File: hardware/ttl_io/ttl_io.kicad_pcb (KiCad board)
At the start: 4 copper layers, 80 x 50 mm, 135 parts, among them J1 Conn_Coaxial, J2 Conn_01x03_Male, J3 Conn_Triaxial, J3 USB_C_Receptacle_USB2.0, J4 AudioJack3, J6 Barrel_Jack_Switch, J7 Conn_Coaxial, SW1 SW_Push, U1 74LVCH2T45DC, U11 LM27762, U12 LT3030, U13 ADS7049, U2 TPD2EUSB30, U3 ADUM4160, U4 RP2040, U5 W25Q16JVUXIQ, U6 LTC6263, U7 LTC6268xS8-10, U8 REF3433QDBVRQ1, U9 AD9833xRM, X1 ECS-TXO-2016

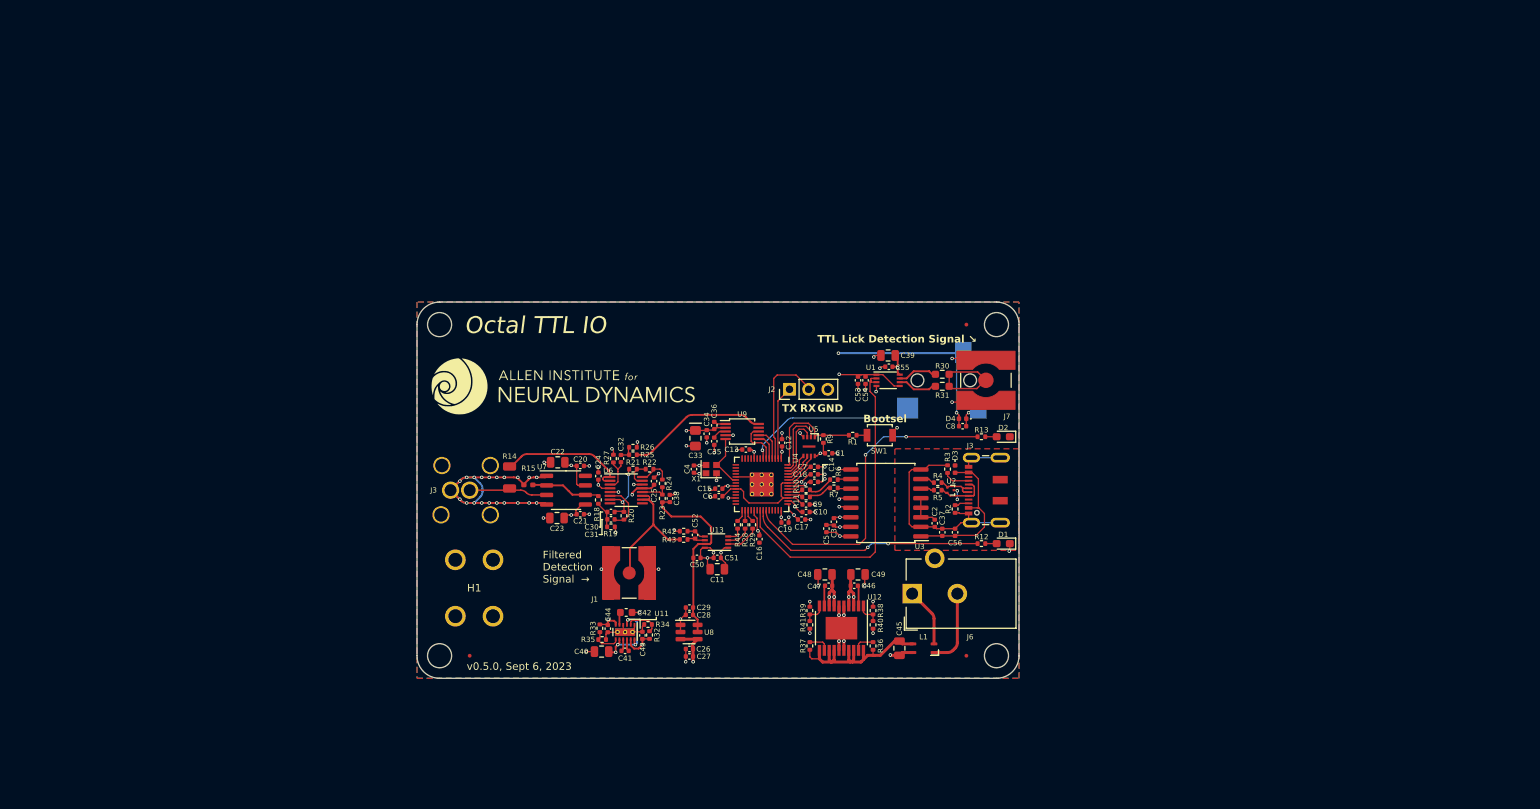
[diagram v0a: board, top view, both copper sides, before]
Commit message: update passthrough level translator
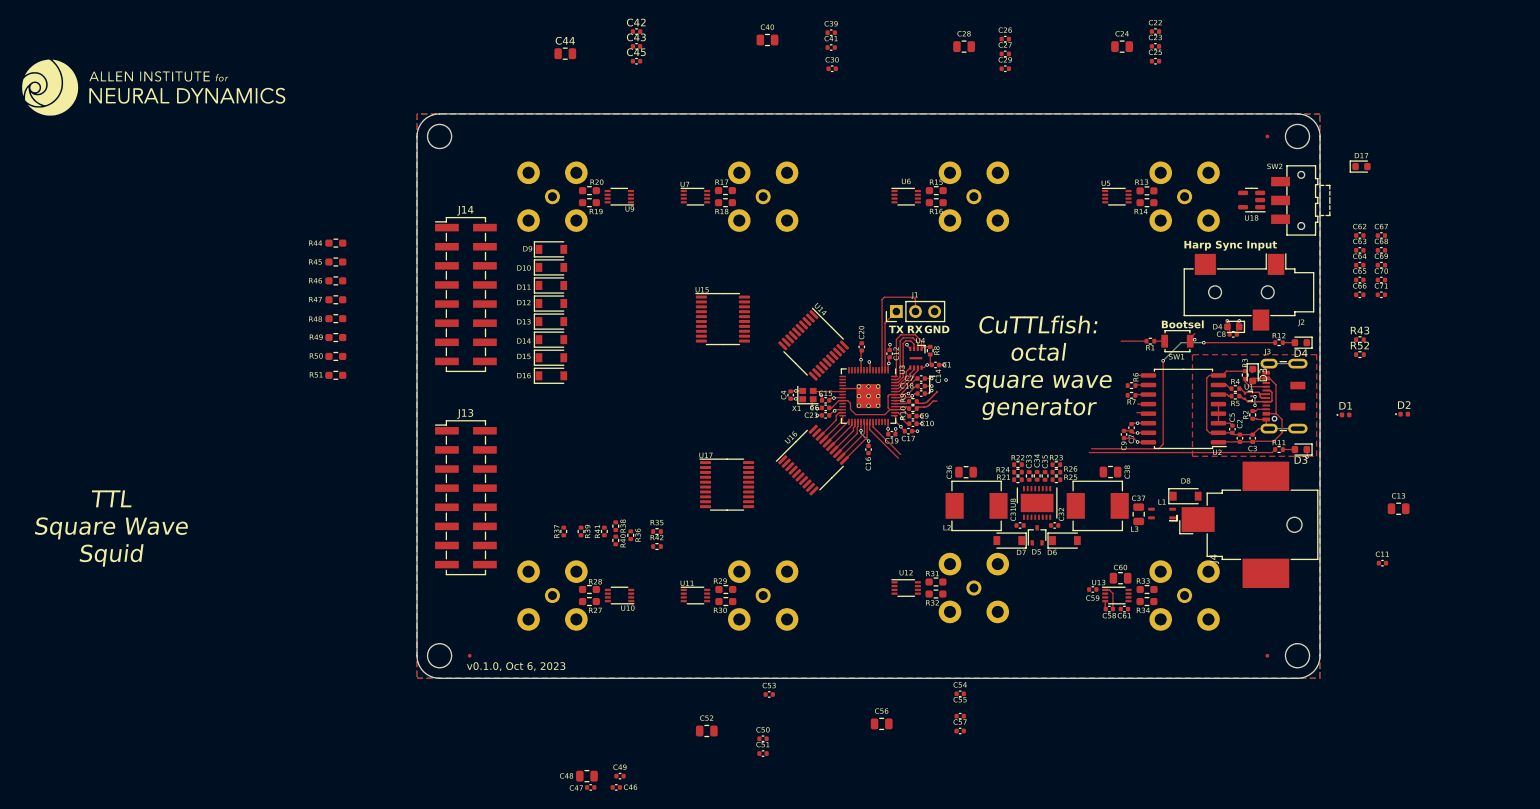
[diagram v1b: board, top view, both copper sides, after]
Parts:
- removed the C20 at (126.6, 89.8)
- removed G1: LOGO, LOGO
- removed H1: MountingHole_Pad, kicad_component_library:Terminal_Keystone_779x_EdgeMount_Horizontal
- removed the J2 at (154.4, 79.6)
- removed the J3 at (111.9, 93.0)
- removed the REF** at (181.9, 115.0)
- removed the REF** at (181.9, 71.0)
- removed the REF** at (107.9, 71.0)
- removed the REF** at (107.9, 115.0)
- removed REF1: OSHW-Logo2_7.3x6mm_SilkScreen, Symbol:OSHW-Logo2_7.3x6mm_SilkScreen
- removed the U1 at (167.5, 78.4)
- added C13: 10uF, Capacitor_SMD:C_0805_2012Metric, F.Cu at (235.3, 95.5)
- added C45: 100nF, Capacitor_SMD:C_0402_1005Metric, F.Cu at (134.1, 36.0)
- added C56: 10uF, Capacitor_SMD:C_0805_2012Metric, F.Cu at (166.7, 124.1)
- added C57: 100nF, Capacitor_SMD:C_0402_1005Metric, F.Cu at (177.1, 125.0)
- added C58: 100nF, Capacitor_SMD:C_0402_1005Metric, F.Cu at (196.9, 108.8)
- added C59: 1uF, Capacitor_SMD:C_0402_1005Metric, F.Cu at (194.7, 106.2)
- added C60: 10uF, Capacitor_SMD:C_0805_2012Metric, F.Cu at (198.4, 104.7)
- added C61: 100nF, Capacitor_SMD:C_0402_1005Metric, F.Cu at (198.9, 108.8)
- added C62: 100nF, Capacitor_SMD:C_0402_1005Metric, F.Cu at (230.2, 59.2)
- added C63: 1uF, Capacitor_SMD:C_0402_1005Metric, F.Cu at (230.2, 61.1)
- added C64: 100nF, Capacitor_SMD:C_0402_1005Metric, F.Cu at (230.2, 63.1)
- added C65: 1uF, Capacitor_SMD:C_0402_1005Metric, F.Cu at (230.2, 65.1)
- added C66: 100nF, Capacitor_SMD:C_0402_1005Metric, F.Cu at (230.2, 67.0)
- added C67: 1uF, Capacitor_SMD:C_0402_1005Metric, F.Cu at (233.1, 59.2)
- added C68: 100nF, Capacitor_SMD:C_0402_1005Metric, F.Cu at (233.1, 61.1)
- added C69: 1uF, Capacitor_SMD:C_0402_1005Metric, F.Cu at (233.1, 63.1)
- added C70: 100nF, Capacitor_SMD:C_0402_1005Metric, F.Cu at (233.1, 65.1)
- added C71: 1uF, Capacitor_SMD:C_0402_1005Metric, F.Cu at (233.1, 67.0)
- added D1: D_TVS, Diode_SMD:D_0402_1005Metric, F.Cu at (228.3, 83.0)
- added D10: D_Schottky, Diode_SMD:D_SOD-123, F.Cu at (122.8, 63.4)
- added D11: D_Schottky, Diode_SMD:D_SOD-123, F.Cu at (122.8, 65.8)
- added D12: D_Schottky, Diode_SMD:D_SOD-123, F.Cu at (122.8, 68.2)
- added D13: D_Schottky, Diode_SMD:D_SOD-123, F.Cu at (122.8, 70.6)
- added D14: D_Schottky, Diode_SMD:D_SOD-123, F.Cu at (122.8, 73.0)
- added D15: D_Schottky, Diode_SMD:D_SOD-123, F.Cu at (122.8, 75.4)
- added D16: D_Schottky, Diode_SMD:D_SOD-123, F.Cu at (122.8, 77.8)
- added D17: LED, LED_SMD:LED_0603_1608Metric, F.Cu at (230.4, 50.0)
- added D2: D_TVS, Diode_SMD:D_0402_1005Metric, F.Cu at (236.1, 82.9)
- added D5: BAT54AW, Package_TO_SOT_SMD:SOT-323_SC-70, F.Cu at (187.3, 99.0)
- added D6: D_Schottky, Diode_SMD:D_SOD-123, F.Cu at (191.0, 99.7)
- added D7: D_Schottky, Diode_SMD:D_SOD-123, F.Cu at (183.6, 99.7)
- added D8: D_Schottky, Diode_SMD:D_SOD-123, F.Cu at (207.1, 93.8)
- added D9: D_Schottky, Diode_SMD:D_SOD-123, F.Cu at (122.8, 61.0)
- added J10: Conn_Coaxial, kicad_component_library:BNC_TEConnectivity_CONBNC001_Vertical, B.Cu at (150.9, 107.0)
- added J11: Conn_Coaxial, kicad_component_library:BNC_TEConnectivity_CONBNC001_Vertical, B.Cu at (178.9, 106.0)
- added J12: Conn_Coaxial, kicad_component_library:BNC_TEConnectivity_CONBNC001_Vertical, B.Cu at (206.9, 107.0)
- added J13: Conn_02x08_Counter_Clockwise, Connector_PinHeader_2.54mm:PinHeader_2x08_P2.54mm_Vertical_SMD, F.Cu at (111.4, 94.0)
- added J14: Conn_02x08_Counter_Clockwise, Connector_PinHeader_2.54mm:PinHeader_2x08_P2.54mm_Vertical_SMD, F.Cu at (111.4, 67.0)
- added J5: Conn_Coaxial, kicad_component_library:BNC_TEConnectivity_CONBNC001_Vertical, B.Cu at (206.9, 54.0)
- added J6: Conn_Coaxial, kicad_component_library:BNC_TEConnectivity_CONBNC001_Vertical, B.Cu at (178.9, 54.0)
- added J8: Conn_Coaxial, kicad_component_library:BNC_TEConnectivity_CONBNC001_Vertical, B.Cu at (122.9, 54.0)
- added J9: Conn_Coaxial, kicad_component_library:BNC_TEConnectivity_CONBNC001_Vertical, B.Cu at (122.9, 107.0)
- added L2: 10uH, Inductor_SMD:L_Vishay_IHLP-2525, F.Cu at (179.3, 95.1)
- added L3: 10uH, Inductor_SMD:L_Vishay_IHLP-2525, F.Cu at (195.4, 95.1)
- added R13: 100, Resistor_SMD:R_0603_1608Metric_Pad0.98x0.95mm_HandSolder, F.Cu at (201.9, 53.2)
- added R16: 100, Resistor_SMD:R_0603_1608Metric_Pad0.98x0.95mm_HandSolder, F.Cu at (173.9, 54.8)
- added R17: 100, Resistor_SMD:R_0603_1608Metric_Pad0.98x0.95mm_HandSolder, F.Cu at (145.9, 53.2)
- added R45: 100, Resistor_SMD:R_0603_1608Metric_Pad0.98x0.95mm_HandSolder, F.Cu at (94.1, 62.7)
- added R46: 100, Resistor_SMD:R_0603_1608Metric_Pad0.98x0.95mm_HandSolder, F.Cu at (94.1, 65.2)
- added R47: 100, Resistor_SMD:R_0603_1608Metric_Pad0.98x0.95mm_HandSolder, F.Cu at (94.1, 67.7)
- added R48: 100, Resistor_SMD:R_0603_1608Metric_Pad0.98x0.95mm_HandSolder, F.Cu at (94.1, 70.2)
- added R49: 100, Resistor_SMD:R_0603_1608Metric_Pad0.98x0.95mm_HandSolder, F.Cu at (94.1, 72.7)
- added R50: 100, Resistor_SMD:R_0603_1608Metric_Pad0.98x0.95mm_HandSolder, F.Cu at (94.1, 75.2)
- added R51: 100, Resistor_SMD:R_0603_1608Metric_Pad0.98x0.95mm_HandSolder, F.Cu at (94.1, 77.7)
- added R52: 1K, Resistor_SMD:R_0402_1005Metric, F.Cu at (230.2, 75.0)
- added REF**: MountingHole_3.2mm_M3_ISO7380, MountingHole:MountingHole_3.2mm_M3_ISO7380, F.Cu at (107.9, 46.0)
- added REF**: MountingHole_3.2mm_M3_ISO7380, MountingHole:MountingHole_3.2mm_M3_ISO7380, F.Cu at (221.9, 46.0)
- added REF**: MountingHole_3.2mm_M3_ISO7380, MountingHole:MountingHole_3.2mm_M3_ISO7380, F.Cu at (107.9, 115.0)
- added REF**: MountingHole_3.2mm_M3_ISO7380, MountingHole:MountingHole_3.2mm_M3_ISO7380, F.Cu at (221.9, 115.0)
- added SW2: SW_SPDT, Button_Switch_SMD:SW_SPDT_CK-JS102011SAQN, F.Cu at (222.4, 54.5)
- added U10: 74LVCH2T45DC, Package_SO:VSSOP-8_2.3x2mm_P0.5mm, F.Cu at (131.8, 107.0)
- added U14: 74CBTLV3245, Package_SO:TSSOP-20_4.4x6.5mm_P0.65mm, F.Cu at (157.6, 73.8)
- added U15: 74CBTLV3245, Package_SO:TSSOP-20_4.4x6.5mm_P0.65mm, F.Cu at (145.6, 70.3)
- added U16: 74CBTLV3245, Package_SO:TSSOP-20_4.4x6.5mm_P0.65mm, F.Cu at (157.6, 89.0)
- added U17: 74CBTLV3245, Package_SO:TSSOP-20_4.4x6.5mm_P0.65mm, F.Cu at (146.1, 92.3)
- added U18: 74LVC1G04, Package_TO_SOT_SMD:SOT-23-5, F.Cu at (215.8, 54.5)
- added U5: 74LVCH2T45DC, Package_SO:VSSOP-8_2.3x2mm_P0.5mm, F.Cu at (197.9, 54.0)
- C11, C23, C39: value 10uF -> 1uF; footprint Capacitor_SMD:C_0805_2012Metric -> Capacitor_SMD:C_0402_1005Metric
- C12, C55: value 100nF -> 1uF
- C2: renamed from C37; value 100nF -> 1uF
- C22: value 10uF -> 100nF; footprint Capacitor_SMD:C_0805_2012Metric -> Capacitor_SMD:C_0402_1005Metric
- C24, C28: value 100nF -> 10uF; footprint Capacitor_SMD:C_0402_1005Metric -> Capacitor_SMD:C_0805_2012Metric
- C29, C41, C53, C8, C9: value 1uF -> 100nF
- C3: renamed from C56; value 1uF -> 100nF
- C30, C31: value 160pF -> 100nF
- C32, C46: value 10nF -> 100nF
- C33: value 10uF -> 1.5nF; footprint Capacitor_SMD:C_0805_2012Metric_Pad1.18x1.45mm_HandSolder -> Resistor_SMD:R_0402_1005Metric
- C34: value 100nF -> 4.7nF; footprint Capacitor_SMD:C_0402_1005Metric -> Resistor_SMD:R_0402_1005Metric
- C35: value 100nF -> 1.5nF; footprint Capacitor_SMD:C_0402_1005Metric -> Resistor_SMD:R_0402_1005Metric
- C36: value 10nF -> 22uF; footprint Capacitor_SMD:C_0402_1005Metric -> Capacitor_SMD:C_0805_2012Metric
- C37: renamed from C45; value 3.3uF -> 10uF
- C38: value 100nF -> 22uF; footprint Capacitor_SMD:C_0402_1005Metric -> Capacitor_SMD:C_0805_2012Metric
- C40: value 22uF -> 10uF
- C42: value 4.7uF -> 100nF; footprint Capacitor_SMD:C_0603_1608Metric -> Capacitor_SMD:C_0402_1005Metric
- C43, C51: value 2.2uF -> 1uF
- C44: value 2.2uF -> 10uF; footprint Capacitor_SMD:C_0402_1005Metric -> Capacitor_SMD:C_0805_2012Metric
- C47: value 10nF -> 1uF
- C49: value 22uF -> 100nF; footprint Capacitor_SMD:C_0805_2012Metric -> Capacitor_SMD:C_0402_1005Metric
- C50: value 2.2uF -> 100nF
- C52: value 300pF -> 10uF; footprint Capacitor_SMD:C_0402_1005Metric -> Capacitor_SMD:C_0805_2012Metric
- D3: renamed from D1; footprint LED_SMD:LED_0603_1608Metric_Pad1.05x0.95mm_HandSolder -> LED_SMD:LED_0603_1608Metric
- D3, D4: value D_TVS -> LED; footprint Diode_SMD:D_0402_1005Metric -> LED_SMD:LED_0603_1608Metric
- D4: renamed from D2; footprint LED_SMD:LED_0603_1608Metric_Pad1.05x0.95mm_HandSolder -> LED_SMD:LED_0603_1608Metric
- J1: value Conn_Coaxial -> Conn_01x03_Male; footprint Connector_Coaxial:SMA_Amphenol_132134-10_Vertical -> Connector_PinHeader_2.54mm:PinHeader_1x03_P2.54mm_Vertical
- J2: renamed from J4; moved to F.Cu
- J4: renamed from J6; footprint Connector_BarrelJack:BarrelJack_CUI_PJ-102AH_Horizontal -> Connector_BarrelJack:BarrelJack_CUI_PJ-036AH-SMT_Horizontal
- J7: footprint kicad_component_library:SMA_TE_Connectivity_CONSMA002-SMD-G-T_Horizontal -> kicad_component_library:BNC_TEConnectivity_CONBNC001_Vertical; moved to B.Cu
- R11: renamed from R12; value 330 -> 680
- R12: renamed from R13; value 330 -> 680
- R14: value 100K -> 100; footprint Resistor_SMD:R_1206_3216Metric -> Resistor_SMD:R_0603_1608Metric_Pad0.98x0.95mm_HandSolder
- R15: footprint Resistor_SMD:R_0402_1005Metric_Pad0.72x0.64mm_HandSolder -> Resistor_SMD:R_0603_1608Metric_Pad0.98x0.95mm_HandSolder
- R18: value 49K9 -> 100; footprint Resistor_SMD:R_0402_1005Metric -> Resistor_SMD:R_0603_1608Metric_Pad0.98x0.95mm_HandSolder
- R19: value 1K02 -> 100; footprint Resistor_SMD:R_0402_1005Metric -> Resistor_SMD:R_0603_1608Metric_Pad0.98x0.95mm_HandSolder
- R20: value 100K -> 100; footprint Resistor_SMD:R_0402_1005Metric -> Resistor_SMD:R_0603_1608Metric_Pad0.98x0.95mm_HandSolder
- R21: value 68 -> 10K
- R24: value 10K -> 31K2
- R26: value 330 -> 52K3
- R27: value 10K -> 100; footprint Resistor_SMD:R_0402_1005Metric -> Resistor_SMD:R_0603_1608Metric_Pad0.98x0.95mm_HandSolder
- R28, R29, R44: value 49.9 -> 100; footprint Resistor_SMD:R_0402_1005Metric -> Resistor_SMD:R_0603_1608Metric_Pad0.98x0.95mm_HandSolder
- R32: value 54K9 -> 100; footprint Resistor_SMD:R_0402_1005Metric -> Resistor_SMD:R_0603_1608Metric_Pad0.98x0.95mm_HandSolder
- R33: value 53K6 -> 100; footprint Resistor_SMD:R_0402_1005Metric -> Resistor_SMD:R_0603_1608Metric_Pad0.98x0.95mm_HandSolder
- R34: value 51K -> 100; footprint Resistor_SMD:R_0402_1005Metric -> Resistor_SMD:R_0603_1608Metric_Pad0.98x0.95mm_HandSolder
- R35: value 51K -> 10K
- R36, R37: value 1M -> 10K
- R38: value 309K -> 10K
- R39: value 172K -> 10K
- R40, R41: value 100K -> 10K
- R42, R43: value 16 -> 10K
- U11: value LM27762 -> 74LVCH2T45DC; footprint Package_SON:WSON-12-1EP_3x2mm_P0.5mm_EP1x2.65_ThermalVias -> Package_SO:VSSOP-8_2.3x2mm_P0.5mm
- U12: value LT3030 -> 74LVCH2T45DC; footprint Package_SO:ETSSOP-20-1EP_4.4x6.5mm_P0.65mm_EP3x4.2mm -> Package_SO:VSSOP-8_2.3x2mm_P0.5mm
- U13: value ADS7049 -> 74LVCH2T45DC
- U6: value LTC6263 -> 74LVCH2T45DC; footprint Package_SO:MSOP-16_3x4mm_P0.5mm -> Package_SO:VSSOP-8_2.3x2mm_P0.5mm
- U7: value LTC6268xS8-10 -> 74LVCH2T45DC; footprint Package_SO:SO-8_3.9x4.9mm_P1.27mm -> Package_SO:VSSOP-8_2.3x2mm_P0.5mm
- U8: value REF3433QDBVRQ1 -> LT3506; footprint Package_TO_SOT_SMD:SOT-23-6 -> Package_DFN_QFN:DFN-16-1EP_4x5mm_P0.5mm_EP2.44x4.34mm
- U9: value AD9833xRM -> 74LVCH2T45DC; footprint Package_SO:MSOP-10_3x3mm_P0.5mm -> Package_SO:VSSOP-8_2.3x2mm_P0.5mm
- moved C23 101.3 mm to (203.0, 34.0), turned to 0 degrees
- moved C22 97.9 mm to (203.0, 32.1)
- moved R43 93.7 mm to (230.2, 73.0)
- moved R14 92.2 mm to (201.9, 54.8), turned to 0 degrees
- moved C26 91.3 mm to (183.1, 33.1)
- moved C27 90.4 mm to (183.1, 35.0), turned to 0 degrees
- moved C24 90.0 mm to (198.6, 34.1), turned to 0 degrees
- moved C11 88.4 mm to (233.2, 102.7), turned to 0 degrees
- moved C25 86.9 mm to (203.0, 36.0), turned to 0 degrees
- moved C41 84.7 mm to (159.9, 34.2), turned to 0 degrees
- moved C40 84.2 mm to (151.5, 33.2), turned to 0 degrees
- moved C28 83.9 mm to (177.6, 34.1)
- moved C29 83.0 mm to (183.1, 37.0), turned to 0 degrees
- moved C43 78.3 mm to (134.1, 34.0), turned to 0 degrees
- moved C42 77.2 mm to (134.1, 32.1)
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- renumbered C13 to C20, C2 to C5, C3 to C7, C5 to C9, R11 to R10, R9 to R8, R10 to R9, U2 to U1, U3 to U2, U4 to U3, U5 to U4
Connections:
- net /Harp Core RP2040 + Isolated USB/D+ renamed /Harp Core Rp2040 + isolated USB/D+
- net /Harp Core RP2040 + Isolated USB/D- renamed /Harp Core Rp2040 + isolated USB/D-
- net /Harp Core RP2040 + Isolated USB/DD+ renamed /Harp Core Rp2040 + isolated USB/DD+
- net /Harp Core RP2040 + Isolated USB/DD- renamed /Harp Core Rp2040 + isolated USB/DD-
- net /Harp Core RP2040 + Isolated USB/HARP_CLK_SYNC renamed /Harp Core Rp2040 + isolated USB/HARP_CLK_SYNC
- net /Harp Core RP2040 + Isolated USB/QSPI_CLK renamed /Harp Core Rp2040 + isolated USB/QSPI_CLK
- net /Harp Core RP2040 + Isolated USB/QSPI_CS renamed /Harp Core Rp2040 + isolated USB/QSPI_CS
- net /Harp Core RP2040 + Isolated USB/QSPI_D0 renamed /Harp Core Rp2040 + isolated USB/QSPI_D0
- net /Harp Core RP2040 + Isolated USB/QSPI_D1 renamed /Harp Core Rp2040 + isolated USB/QSPI_D1
- net /Harp Core RP2040 + Isolated USB/QSPI_D2 renamed /Harp Core Rp2040 + isolated USB/QSPI_D2
- net /Harp Core RP2040 + Isolated USB/QSPI_D3 renamed /Harp Core Rp2040 + isolated USB/QSPI_D3
- net /Harp Core RP2040 + Isolated USB/USB_Boot renamed /Harp Core Rp2040 + isolated USB/USB_Boot
- net /Harp Core RP2040 + Isolated USB/VDD1 renamed /Harp Core Rp2040 + isolated USB/VDD1
- C10 pad 1: +3V3 -> +1V1
- C12 pad 1: GND -> +3V3
- C12 pad 2: +3V3 -> GND
- C2 pad 1: GND1 -> VBUS
- C2 pad 2: VBUS -> GND1
- C21 pad 1: -2V5 -> GND
- C21 pad 2: GND -> +3V3
- C22 pad 2: +2V5 -> +3V3
- C23 pad 1: -2V5 -> +3V3
- C24 pad 1: GND -> +5V
- C24 pad 2: +2V5 -> GND
- C25 pad 1: -2V5 -> GND
- C25 pad 2: GND -> +5V
- C26 pad 2: +5V -> +3V3
- C27 pad 1: +5V -> +3V3
- C28 pad 1: GND -> +5V
- C28 pad 2: VREF_3V3 -> GND
- C29 pad 1: VREF_3V3 -> GND
- C29 pad 2: GND -> +5V
- C3 pad 1: VBUS -> GND1
- C3 pad 2: GND1 -> VBUS
- C30 pad 1: Net-(C30-Pad1) -> GND
- C30 pad 2: Net-(C30-Pad2) -> +3V3
- C31 pad 1: Net-(C30-Pad1) -> Net-(D7-K)
- C31 pad 2: Net-(U6B--) -> Net-(U8-BOOST1)
- C32 pad 1: Net-(C32-Pad1) -> Net-(D6-K)
- C32 pad 2: Net-(U6A-+) -> Net-(U8-BOOST2)
- C33 pad 1: +3V3 -> Net-(C33-Pad1)
- C33 pad 2: GND -> Net-(U8-VC1)
- C34 pad 2: +3V3 -> Net-(U8-RUN/SS1)
- C35 pad 1: GND -> Net-(U8-VC2)
- C35 pad 2: Net-(U9-CAP/2.5V) -> Net-(C35-Pad2)
- C36 pad 1: Net-(U9-COMP) -> +3V3
- C36 pad 2: +3V3 -> GND
- C37 pad 1: IN1 -> VIN1
- C38 pad 1: GND -> +5V
- C38 pad 2: VREF_3V3 -> GND
- C39 pad 1: +5V -> +3V3
- C41 pad 1: Net-(U11-C+) -> GND
- C41 pad 2: Net-(U11-C-) -> +5V
- C42 pad 1: Net-(U11-CP) -> GND
- C42 pad 2: GND -> +3V3
- C43 pad 1: GND -> +3V3
- C43 pad 2: +2V5 -> GND
- C44 pad 1: GND -> +5V
- C44 pad 2: -2V5 -> GND
- C46 pad 1: +5V -> GND
- C46 pad 2: Net-(U12-BYP1) -> +3V3
- C47 pad 2: Net-(U12-BYP2) -> GND
- C48 pad 1: +3V3 -> +5V
- C49 pad 1: +5V -> GND
- C49 pad 2: GND -> +5V
- C50 pad 2: VREF_3V3 -> +3V3
- C51 pad 1: GND -> +3V3
- C51 pad 2: +3V3 -> GND
- C52 pad 1: Net-(U13-AINP) -> +5V
- C52 pad 2: Net-(U13-AINM) -> GND
- C53 pad 1: +3V3 -> GND
- C53 pad 2: GND -> +5V
- C55 pad 1: GND -> +3V3
- C55 pad 2: +5V -> GND
- C7 pad 2: +1V1 -> +3V3
- C8 pad 1: +3V3 -> GND
- C8 pad 2: GND -> +1V1
- C9 pad 1: +1V1 -> GND
- C9 pad 2: GND -> +3V3
- D3 pad 2: Net-(D1-A) -> Net-(D3-A)
- D3 pad 1: GND1 -> GND
- D3 pad 2: VBUS -> Net-(D3-A)
- D4 pad 2: Net-(D2-A) -> Net-(D4-A)
- D4 pad 2: +3V3 -> Net-(D4-A)
- J1 pad 1: Net-(J1-In) -> /Harp Core Rp2040 + isolated USB/UART0_TXD
- J1 pad 2: GND -> /Harp Core Rp2040 + isolated USB/UART0_RXD
- L1 pad 2: +12V -> Net-(D8-K)
- L1 pad 3: IN1 -> VIN1
- R11 pad 2: Net-(D1-A) -> Net-(D3-A)
- R12 pad 2: Net-(D2-A) -> Net-(D4-A)
- R14 pad 1: /100KHz Sine Wave/VSINE -> Net-(U5-2B)
- R14 pad 2: /Lick Detection Analog Front End/triax_core -> Net-(J5-In)
- R15 pad 1: /Lick Detection Analog Front End/triax_inner_shield -> Net-(U6-1B)
- R15 pad 2: Net-(U7--) -> Net-(J6-In)
- R18 pad 1: Net-(U7--) -> Net-(U7-2B)
- R18 pad 2: Net-(C30-Pad1) -> Net-(J7-In)
- R19 pad 1: GND -> Net-(U9-1B)
- R19 pad 2: Net-(C30-Pad1) -> Net-(J8-In)
- R20 pad 1: Net-(U6B--) -> Net-(U9-2B)
- R20 pad 2: Net-(C30-Pad2) -> Net-(J8-In)
- R21 pad 1: Net-(C30-Pad2) -> Net-(U8-FB1)
- R21 pad 2: Net-(U6D--) -> +3V3
- R22 pad 1: Net-(U6D--) -> GND
- R22 pad 2: Net-(R22-Pad2) -> Net-(C33-Pad1)
- R23 pad 1: Net-(U6C-+) -> GND
- R23 pad 2: VREF_3V3 -> Net-(C35-Pad2)
- R24 pad 1: Net-(R22-Pad2) -> Net-(U8-FB1)
- R24 pad 2: Net-(U6C-+) -> GND
- R25 pad 1: Net-(C32-Pad1) -> +5V
- R25 pad 2: Net-(U9-VOUT) -> Net-(U8-FB2)
- R26 pad 1: Net-(C32-Pad1) -> GND
- R26 pad 2: GND -> Net-(U8-FB2)
- R27 pad 1: GND -> Net-(U10-1B)
- R27 pad 2: Net-(U6A-+) -> Net-(J9-In)
- R28 pad 1: Net-(U13-SDO) -> Net-(U10-2B)
- R28 pad 2: /Harp Core RP2040 + Isolated USB/PIO_POCI -> Net-(J9-In)
- R29 pad 1: Net-(U13-SCLK) -> Net-(U11-1B)
- R29 pad 2: /Harp Core RP2040 + Isolated USB/PIO_SCK -> Net-(J10-In)
- R30 pad 1: Net-(U1-1B) -> Net-(U11-2B)
- R30 pad 2: Net-(J7-In) -> Net-(J10-In)
- R31 pad 1: Net-(U1-2B) -> Net-(U12-1B)
- R31 pad 2: Net-(J7-In) -> Net-(J11-In)
- R32 pad 1: +2V5 -> Net-(U12-2B)
- R32 pad 2: Net-(U11-FB+) -> Net-(J11-In)
- R33 pad 1: -2V5 -> Net-(U13-1B)
- R33 pad 2: Net-(U11-FB-) -> Net-(J12-In)
- R34 pad 1: Net-(U11-FB+) -> Net-(U13-2B)
- R34 pad 2: GND -> Net-(J12-In)
- R35 pad 1: Net-(U11-FB-) -> /EXT_DIR0
- R35 pad 2: GND -> +3V3
- R36 pad 1: IN1 -> /EXT_DIR1
- R36 pad 2: Net-(U12-PWRGD1) -> +3V3
- R37 pad 1: IN1 -> /EXT_DIR2
- R37 pad 2: Net-(U12-PWRGD2) -> +3V3
- R38 pad 1: +5V -> /EXT_DIR3
- R38 pad 2: Net-(U12-ADJ1) -> +3V3
- R39 pad 1: +3V3 -> /EXT_DIR4
- R39 pad 2: Net-(U12-ADJ2) -> +3V3
- R40 pad 1: GND -> /EXT_DIR5
- R40 pad 2: Net-(U12-ADJ1) -> +3V3
- R41 pad 1: GND -> /EXT_DIR6
- R41 pad 2: Net-(U12-ADJ2) -> +3V3
- R42 pad 1: Net-(U13-AINM) -> /EXT_DIR7
- R42 pad 2: GND -> +3V3
- R43 pad 1: Net-(J1-In) -> /HARP_CTRL
- R43 pad 2: Net-(U13-AINP) -> +3V3
- R44 pad 1: Net-(U13-~{CS}) -> Net-(J14-Pin_1)
- R44 pad 2: /Harp Core RP2040 + Isolated USB/PIO_CS -> /EXT_IN0
- U11 pad 1: GND -> +3V3
- U11 pad 2: Net-(U11-FB+) -> /TTL5
- U11 pad 3: +5V -> /TTL5
- U11 pad 5: Net-(U11-CP) -> /TTL_DIR5
- U11 pad 6: -2V5 -> Net-(U11-2B)
- U11 pad 7: Net-(U11-FB-) -> Net-(U11-1B)
- U12 pad 1: Net-(U12-ADJ1) -> +3V3
- U12 pad 2: Net-(U12-BYP1) -> /TTL6
- U12 pad 3: +5V -> /TTL6
- U12 pad 4: +5V -> GND
- U12 pad 5: GND -> /TTL_DIR6
- U12 pad 6: GND -> Net-(U12-2B)
- U12 pad 7: +3V3 -> Net-(U12-1B)
- U12 pad 8: +3V3 -> +5V
- U13 pad 2: Net-(U13-SCLK) -> /TTL7
- U13 pad 3: Net-(U13-SDO) -> /TTL7
- U13 pad 4: Net-(U13-~{CS}) -> GND
- U13 pad 5: Net-(U13-AINM) -> /TTL_DIR7
- U13 pad 6: Net-(U13-AINP) -> Net-(U13-2B)
- U13 pad 7: VREF_3V3 -> Net-(U13-1B)
- U13 pad 8: GND -> +5V
- U3 pad 11: unconnected-(U4-GPIO8-Pad11) -> /INT_IN0
- U3 pad 12: unconnected-(U4-GPIO9-Pad12) -> /INT_IN1
- U3 pad 13: unconnected-(U4-GPIO10-Pad13) -> /INT_IN2
- U3 pad 14: unconnected-(U4-GPIO11-Pad14) -> /INT_IN3
- U3 pad 15: unconnected-(U4-GPIO12-Pad15) -> /INT_IN4
- U3 pad 16: unconnected-(U4-GPIO13-Pad16) -> /INT_IN5
- U3 pad 17: unconnected-(U4-GPIO14-Pad17) -> /INT_IN6
- U3 pad 18: unconnected-(U4-GPIO15-Pad18) -> /INT_IN7
- U3 pad 2: /Harp Core RP2040 + Isolated USB/UART0_TXD -> /Harp Core Rp2040 + isolated USB/UART0_TXD
- U3 pad 20: /100KHz Sine Wave/xtal_in -> Net-(U3-XIN)
- U3 pad 24: /Harp Core RP2040 + Isolated USB/SWCLK -> unconnected-(U3-SWCLK-Pad24)
- U3 pad 25: /Harp Core RP2040 + Isolated USB/SWDIO -> unconnected-(U3-SWD-Pad25)
- U3 pad 27: unconnected-(U4-GPIO16-Pad27) -> /INT_DIR0
- U3 pad 28: unconnected-(U4-GPIO17-Pad28) -> /INT_DIR1
- U3 pad 29: /Harp Core RP2040 + Isolated USB/PIO_CS -> /INT_DIR2
- U3 pad 3: /Harp Core RP2040 + Isolated USB/UART0_RXD -> /Harp Core Rp2040 + isolated USB/UART0_RXD
- U3 pad 30: /Harp Core RP2040 + Isolated USB/PIO_POCI -> /INT_DIR3
- U3 pad 31: /Harp Core RP2040 + Isolated USB/PIO_SCK -> /INT_DIR4
- U3 pad 32: unconnected-(U4-GPIO21-Pad32) -> /INT_DIR5
- U3 pad 34: unconnected-(U4-GPIO22-Pad34) -> /INT_DIR6
- U3 pad 35: /Harp Core RP2040 + Isolated USB/TTL_OUT -> /INT_DIR7
- U3 pad 4: /100KHz Sine Wave/SCK -> unconnected-(U3-GPIO2-Pad4)
- U3 pad 5: /100KHz Sine Wave/PICO -> unconnected-(U3-GPIO3-Pad5)
- U3 pad 6: /100KHz Sine Wave/CS -> unconnected-(U3-GPIO4-Pad6)
- U6 pad 1: /100KHz Sine Wave/VSINE -> +3V3
- U6 pad 2: /100KHz Sine Wave/VSINE -> /TTL1
- U6 pad 3: Net-(U6A-+) -> /TTL1
- U6 pad 4: +2V5 -> GND
- U6 pad 5: GND -> /TTL_DIR1
- U6 pad 6: Net-(U6B--) -> Net-(U6-2B)
- U6 pad 7: Net-(C30-Pad2) -> Net-(U6-1B)
- U6 pad 8: unconnected-(U6E-NC-Pad8) -> +5V
- U7 pad 1: /Lick Detection Analog Front End/triax_inner_shield -> +3V3
- U7 pad 2: Net-(U7--) -> /TTL2
- U7 pad 3: /Lick Detection Analog Front End/triax_core -> /TTL2
- U7 pad 4: /Lick Detection Analog Front End/triax_inner_shield -> GND
- U7 pad 5: -2V5 -> /TTL_DIR2
- U7 pad 6: Net-(U7--) -> Net-(U7-2B)
- U7 pad 7: +2V5 -> Net-(U7-1B)
- U7 pad 8: unconnected-(U7-~{SHDN}-Pad8) -> +5V
- U8 pad 1: GND -> Net-(U8-BOOST1)
- U8 pad 2: GND -> Net-(D7-K)
- U8 pad 3: +5V -> VIN1
- U8 pad 4: +5V -> VIN1
- U8 pad 5: VREF_3V3 -> VIN1
- U8 pad 6: VREF_3V3 -> VIN1
- U9 pad 1: Net-(U9-COMP) -> +3V3
- U9 pad 2: +3V3 -> /TTL3
- U9 pad 3: Net-(U9-CAP/2.5V) -> /TTL3
- U9 pad 5: /100KHz Sine Wave/xtal_in -> /TTL_DIR3
- U9 pad 6: /100KHz Sine Wave/PICO -> Net-(U9-2B)
- U9 pad 7: /100KHz Sine Wave/SCK -> Net-(U9-1B)
- U9 pad 8: /100KHz Sine Wave/CS -> +5V
- X1 pad 3: /100KHz Sine Wave/xtal_in -> Net-(U3-XIN)
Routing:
- net GND: track 98.8 -> 24.7 mm, vias 61 -> 19
- net +3V3: track 90.6 -> 45.7 mm, vias 24 -> 17
- net /Harp Core RP2040 + Isolated USB/TTL_OUT: track 44.5 -> 0.00 mm
- net /Lick Detection Analog Front End/triax_inner_shield: track 39.7 -> 0.00 mm, vias 20 -> 0
- net +5V: track 27.6 -> 0.00 mm, vias 9 -> 0
- net IN1: track 26.0 -> 0.00 mm
- net VREF_3V3: track 25.1 -> 0.00 mm
- net /Harp Core Rp2040 + isolated USB/HARP_CLK_SYNC: track 23.1 -> 1.14 mm
- net Net-(J1-In): track 18.7 -> 0.00 mm
- net Net-(U9-VOUT): track 18.6 -> 0.00 mm
- net /100KHz Sine Wave/VSINE: track 17.8 -> 0.00 mm
- net /Harp Core RP2040 + Isolated USB/UART0_RXD: track 16.5 -> 0.00 mm
- net /Harp Core Rp2040 + isolated USB/UART0_RXD: track 0.00 -> 15.7 mm
- net Net-(J7-In): track 12.5 -> 0.00 mm
- net +2V5: track 12.2 -> 0.00 mm, vias 3 -> 0
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- removed copper zone on In2.Cu, net +2V5
- removed copper zone on In2.Cu, net -2V5
- removed copper zone on In1.Cu, net /Lick Detection Analog Front End/triax_inner_shield
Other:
- board size 80 x 50 mm -> 120 x 75 mm
- board text added: "CuTTLfish can be used in two ways: 1.) as a programmable square wave generator with 8 TTL outputs. 2.) as a TTl buffer for 3.3V logic (input and output)"
- board text added: "CuTTLfish: octal square wave generator"
- board text added: "Hammond: 1455J1202BK"
- board text added: "Harp Sync Input"
- board text added: "Programmable Square Wave Generator and general purpose TTL input/output."
- board text added: "Setup Notes: • Slide the switch <DIRECTION> to enable USB control of the BNC connections. • Slide the switch <DIRECTION> to enable external control of the BNC connections."
- board text added: "Sonya Vasquez"
- board text added: "TODO: Connector heights. * Do the passthrough pins and power jack need to go on the bottom? OR * Put everything on top except the BNC connectors?"
- board text added: "TODO: TVS diodes on all BNC inputs."
- board text added: "TTL Square Wave Squid"
- board text added: "v0.1.0, Oct 6, 2023"
- board text removed: "Chassis Ground"
- board text removed: "Filtered Detection Signal →"
- board text removed: "Fits in enclosure: 1457C801E or 1457C801EBK"
- board text removed: "Harp Sync Input ↑"
- board text removed: "Lick Tube Input ↑"
- board text removed: "Octal TTL IO"
- board text removed: "Setup Notes: • The ground lug must be connected to the chassis ground of the rig. • USB and 3.5mm (Harp) connections are not needed if solely using the TTL output."
- board text removed: "Sub-millisecond, ephys-compatible rodent lick detection system."
- board text removed: "TTL Lick Detection Signal ↘"
- board text removed: "Vasquez"
- board text removed: "v0.5.0, Sept 6, 2023"

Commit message: update layout
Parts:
- removed D13, D14, D15, D16: D_Schottky, Diode_SMD:D_SOD-123
- removed D17: LED, LED_SMD:LED_0603_1608Metric
- removed the D4 at (213.4, 71.3)
- removed R49, R50, R51: 100, Resistor_SMD:R_0603_1608Metric_Pad0.98x0.95mm_HandSolder
- removed R52: 1K, Resistor_SMD:R_0402_1005Metric
- added C72: 100nF, Capacitor_SMD:C_0402_1005Metric, F.Cu at (140.8, 60.5)
- added C73: 1uF, Capacitor_SMD:C_0402_1005Metric, F.Cu at (140.8, 59.4)
- added C74: 100nF, Capacitor_SMD:C_0402_1005Metric, F.Cu at (234.0, 49.4)
- added C75: 100nF, Capacitor_SMD:C_0402_1005Metric, F.Cu at (233.8, 55.6)
- added C76: 100nF, Capacitor_SMD:C_0402_1005Metric, F.Cu at (233.8, 60.7)
- added C77: 100nF, Capacitor_SMD:C_0402_1005Metric, F.Cu at (236.3, 40.3)
- added SW3: SW_SPDT, Button_Switch_SMD:SW_SPDT_CK-JS102011SAQN, F.Cu at (106.7, 80.6)
- added U19: TXB0108DQSR, Package_SON:USON-20_2x4mm_P0.4mm, F.Cu at (149.0, 67.9)
- D10, D11, D12: value D_Schottky -> NSR05F40NXT5G; footprint Diode_SMD:D_SOD-123 -> Diode_SMD:D_0402_1005Metric
- D9: value D_Schottky -> LED; footprint Diode_SMD:D_SOD-123 -> LED_SMD:LED_0603_1608Metric
- J13, J14: footprint Connector_PinHeader_2.54mm:PinHeader_2x08_P2.54mm_Vertical_SMD -> kicad_component_library:PinHeader_2x08_P2.54mm_Horizontal_SMD
- R13, R14, R15, R16, R17, R18, R19, R20, R27, R28, R29, R30, R31, R32, R33, R34: footprint Resistor_SMD:R_0603_1608Metric_Pad0.98x0.95mm_HandSolder -> Resistor_SMD:R_0402_1005Metric
- R43: value 10K -> 1K
- R44, R45, R46, R47: value 100 -> 10K; footprint Resistor_SMD:R_0603_1608Metric_Pad0.98x0.95mm_HandSolder -> Resistor_SMD:R_0402_1005Metric
- R48: value 100 -> 47K; footprint Resistor_SMD:R_0603_1608Metric_Pad0.98x0.95mm_HandSolder -> Resistor_SMD:R_0402_1005Metric
- U15: value 74CBTLV3245 -> SN74LVC1G14DRL; footprint Package_SO:TSSOP-20_4.4x6.5mm_P0.65mm -> Package_TO_SOT_SMD:SOT-553
- moved R47 149.9 mm to (242.9, 49.5)
- moved R48 145.1 mm to (236.3, 41.3)
- moved R44 143.3 mm to (236.3, 42.3), turned to 180 degrees
- moved R45 139.8 mm to (233.8, 57.6)
- moved R46 139.7 mm to (233.8, 62.7)
- moved D12 128.6 mm to (250.9, 57.5)
- moved D10 111.3 mm to (233.8, 56.6)
- moved D11 111.1 mm to (233.8, 61.7), turned to 180 degrees
- moved D9 100.1 mm to (222.8, 60.3), turned to 180 degrees
- moved U15 93.1 mm to (234.0, 41.3), turned to 180 degrees
- moved C68 89.1 mm to (148.2, 88.2)
- moved C69 88.2 mm to (148.2, 87.2), turned to 180 degrees
- moved C63 87.2 mm to (143.1, 66.5), turned to -90 degrees
- moved C62 85.6 mm to (144.9, 66.5), turned to 90 degrees
- moved C64 79.6 mm to (153.7, 85.5), turned to 45 degrees
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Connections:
- D10 pad 1: +3V3 -> ~{EXT_CTRL}
- D10 pad 2: /EXT_IN1 -> Net-(D10-A)
- D11 pad 1: +3V3 -> Net-(D11-K)
- D11 pad 2: /EXT_IN2 -> EXT_CTRL
- D12 pad 1: +3V3 -> ~{HARP_CTRL}
- D12 pad 2: /EXT_IN3 -> Net-(D11-K)
- D9 pad 1: +3V3 -> Net-(D9-K)
- D9 pad 2: /EXT_IN0 -> Net-(D9-A)
- J13 pad 1: /EXT_DIR0 -> GND
- J13 pad 10: GND -> /EXT_DIR6
- J13 pad 11: GND -> /EXT_DIR5
- J13 pad 12: GND -> /EXT_DIR4
- J13 pad 13: GND -> /EXT_DIR3
- J13 pad 14: GND -> /EXT_DIR2
- J13 pad 15: GND -> /EXT_DIR1
- J13 pad 16: GND -> /EXT_DIR0
- J13 pad 2: /EXT_DIR1 -> GND
- J13 pad 3: /EXT_DIR2 -> GND
- J13 pad 4: /EXT_DIR3 -> GND
- J13 pad 5: /EXT_DIR4 -> GND
- J13 pad 6: /EXT_DIR5 -> GND
- J13 pad 7: /EXT_DIR6 -> GND
- J13 pad 8: /EXT_DIR7 -> GND
- J13 pad 9: GND -> /EXT_DIR7
- J14 pad 1: Net-(J14-Pin_1) -> GND
- J14 pad 10: GND -> /EXT_IN6
- J14 pad 11: GND -> /EXT_IN5
- J14 pad 12: GND -> /EXT_IN4
- J14 pad 13: GND -> /EXT_IN3
- J14 pad 14: GND -> /EXT_IN2
- J14 pad 15: GND -> /EXT_IN1
- J14 pad 16: GND -> /EXT_IN0
- J14 pad 2: Net-(J14-Pin_2) -> GND
- J14 pad 3: Net-(J14-Pin_3) -> GND
- J14 pad 4: Net-(J14-Pin_4) -> GND
- J14 pad 5: Net-(J14-Pin_5) -> GND
- J14 pad 6: Net-(J14-Pin_6) -> GND
- J14 pad 7: Net-(J14-Pin_7) -> GND
- J14 pad 8: Net-(J14-Pin_8) -> GND
- J14 pad 9: GND -> /EXT_IN7
- R43 pad 1: /HARP_CTRL -> Net-(D9-A)
- R44 pad 1: Net-(J14-Pin_1) -> Net-(D9-K)
- R44 pad 2: /EXT_IN0 -> +3V3
- R45 pad 1: Net-(J14-Pin_2) -> ~{HARP_CTRL}
- R45 pad 2: /EXT_IN1 -> Net-(D11-K)
- R46 pad 1: Net-(J14-Pin_3) -> ~{EXT_CTRL}
- R46 pad 2: /EXT_IN2 -> Net-(D10-A)
- R47 pad 1: Net-(J14-Pin_4) -> EXT_CTRL
- R47 pad 2: /EXT_IN3 -> Net-(D11-K)
- R48 pad 1: Net-(J14-Pin_5) -> Net-(C77-Pad2)
- R48 pad 2: /EXT_IN4 -> Net-(D9-K)
- SW2 pad 2: /HARP_CTRL -> Net-(D9-K)
- U14 pad 19: /HARP_CTRL -> ~{HARP_CTRL}
- U15 pad 2: /EXT_IN0 -> Net-(C77-Pad2)
- U15 pad 3: /EXT_IN1 -> GND
- U15 pad 4: /EXT_IN2 -> Net-(D11-K)
- U15 pad 5: /EXT_IN3 -> +3V3
- U16 pad 19: /HARP_CTRL -> ~{HARP_CTRL}
- U17 pad 19: /EXT_CTRL -> ~{EXT_CTRL}
- U18 pad 2: /HARP_CTRL -> Net-(D11-K)
- U18 pad 4: /EXT_CTRL -> Net-(D10-A)
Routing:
- net Net-(SW3-B): track 0.00 -> 42.5 mm, vias 0 -> 2
- net /EXT_DIR7: track 0.00 -> 42.3 mm, vias 0 -> 2
- net /EXT_DIR6: track 0.00 -> 40.2 mm, vias 0 -> 2
- net /EXT_DIR5: track 0.00 -> 38.4 mm, vias 0 -> 2
- net /EXT_DIR4: track 0.00 -> 37.0 mm, vias 0 -> 2
- net /EXT_DIR3: track 0.00 -> 35.6 mm, vias 0 -> 2
- net /EXT_DIR2: track 0.00 -> 34.2 mm, vias 0 -> 2
- net /EXT_DIR1: track 0.00 -> 32.7 mm, vias 0 -> 2
- net /EXT_DIR0: track 0.00 -> 32.4 mm, vias 0 -> 1
- net /EXT_IN7: track 0.00 -> 31.9 mm
- net /EXT_IN0: track 0.00 -> 31.5 mm
- net /EXT_IN6: track 0.00 -> 31.0 mm
- net /EXT_IN1: track 0.00 -> 30.6 mm
- net /EXT_IN5: track 0.00 -> 30.1 mm
- net /EXT_IN2: track 0.00 -> 29.7 mm
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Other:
- board text added: "IO0"
- board text added: "IO1"
- board text added: "IO2"
- board text added: "IO3"
- board text added: "IO4"
- board text added: "IO5"
- board text added: "IO6"
- board text added: "IO7"
- board text added: "TODO: Connector heights. * Put everything on top except the BNC connectors?"
- board text added: "TODO: TVS diodes on all BNC inputs? TODO: Switch BOOTSEL switch for washable variant."
- board text added: "cuTTLfish: octal square wave generator"
- board text added: "v0.1.0, Nov 7, 2023"
- board text removed: "CuTTLfish: octal square wave generator"
- board text removed: "TODO: Connector heights. * Do the passthrough pins and power jack need to go on the bottom? OR * Put everything on top except the BNC connectors?"
- board text removed: "TODO: TVS diodes on all BNC inputs."
- board text removed: "v0.1.0, Oct 6, 2023"
